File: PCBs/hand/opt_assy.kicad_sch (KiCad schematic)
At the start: 4 parts

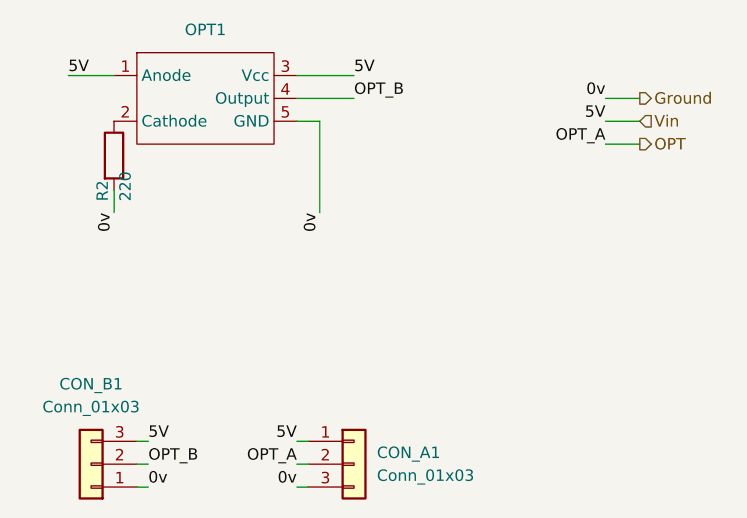
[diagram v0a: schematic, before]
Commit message: Separated Hand B as separate Kicad project. Next up: gerber generation
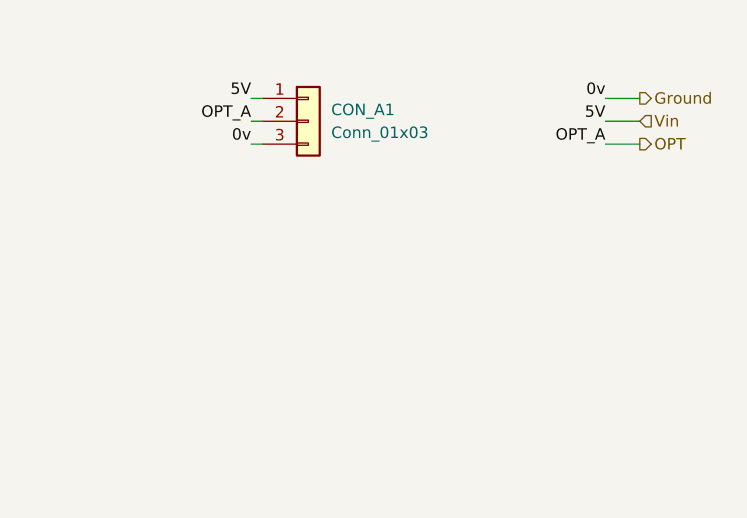
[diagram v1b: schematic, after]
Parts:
- removed CON_B1: Conn_01x03, Connector_PinHeader_2.54mm:PinHeader_1x03_P2.54mm_Vertical, symbol Connector_Generic:Conn_01x03
- removed OPT1: ~, OPB971N51:OPB971N51, symbol OPB971N51:OPB971N51
- removed R2: 220, Resistor_SMD:R_0402_1005Metric, symbol Device:R
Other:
- moved on the sheet: CON_A1
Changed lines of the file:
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@@
 (kicad_sch (version 20230121) (generator eeschema)
   (paper "A5")
-  (wire (pts (xy 85.09 52.07) (xy 85.09 49.53))
-    (stroke (width 0) (type default))
-  )
-  (wire (pts (xy 87.63 80.01) (xy 88.9 80.01))
-    (stroke (width 0) (type default))
-  )
-  (wire (pts (xy 87.63 82.55) (xy 88.9 82.55))
-    (stroke (width 0) (type default))
-  )
-  (wire (pts (xy 105.41 39.37) (xy 111.76 39.37))
-    (stroke (width 0) (type default))
-  )
-  (wire (pts (xy 105.41 36.83) (xy 111.76 36.83))
-    (stroke (width 0) (type default))
-  )
-  (wire (pts (xy 105.41 77.47) (xy 106.68 77.47))
+  (wire (pts (xy 100.33 39.37) (xy 101.6 39.37))
     (stroke (width 0) (type default))
   )
@@
     (stroke (width 0) (type default))
   )
-  (wire (pts (xy 107.95 41.91) (xy 107.95 52.07))
-    (stroke (width 0) (type default))
-  )
-  (wire (pts (xy 105.41 80.01) (xy 106.68 80.01))
+  (wire (pts (xy 100.33 41.91) (xy 101.6 41.91))
     (stroke (width 0) (type default))
   )
@@
     (stroke (width 0) (type default))
   )
-  (wire (pts (xy 87.63 77.47) (xy 88.9 77.47))
-    (stroke (width 0) (type default))
-  )
   (wire (pts (xy 139.7 41.91) (xy 143.51 41.91))
     (stroke (width 0) (type default))
   )
-  (wire (pts (xy 80.01 36.83) (xy 85.09 36.83))
+  (wire (pts (xy 100.33 44.45) (xy 101.6 44.45))
     (stroke (width 0) (type default))
   )
-  (wire (pts (xy 105.41 41.91) (xy 107.95 41.91))
-    (stroke (width 0) (type default))
-  )
-  (wire (pts (xy 105.41 82.55) (xy 106.68 82.55))
-    (stroke (width 0) (type default))
-  )
-  (label "0v" (at 105.41 82.55 180) (fields_autoplaced)
+  (label "0v" (at 100.33 44.45 180) (fields_autoplaced)
     (effects (font (size 1.27 1.27)) (justify right bottom))
   )
-  (label "OPT_B" (at 111.76 39.37 0) (fields_autoplaced)
-    (effects (font (size 1.27 1.27)) (justify left bottom))
-  )
-  (label "OPT_A" (at 105.41 80.01 180) (fields_autoplaced)
+  (label "OPT_A" (at 100.33 41.91 180) (fields_autoplaced)
     (effects (font (size 1.27 1.27)) (justify right bottom))
-  )
-  (label "5V" (at 111.76 36.83 0) (fields_autoplaced)
-    (effects (font (size 1.27 1.27)) (justify left bottom))
-  )
-  (label "5V" (at 88.9 77.47 0) (fields_autoplaced)
-    (effects (font (size 1.27 1.27)) (justify left bottom))
   )
   (label "5V" (at 139.7 41.91 180) (fields_autoplaced)
     (effects (font (size 1.27 1.27)) (justify right bottom))
   )
-  (label "0v" (at 88.9 82.55 0) (fields_autoplaced)
-    (effects (font (size 1.27 1.27)) (justify left bottom))
-  )
-  (label "OPT_B" (at 88.9 80.01 0) (fields_autoplaced)
-    (effects (font (size 1.27 1.27)) (justify left bottom))
-  )
-  (label "5V" (at 105.41 77.47 180) (fields_autoplaced)
+  (label "5V" (at 100.33 39.37 180) (fields_autoplaced)
     (effects (font (size 1.27 1.27)) (justify right bottom))
   )
@@
     (effects (font (size 1.27 1.27)) (justify right bottom))
   )
-  (label "0v" (at 107.95 52.07 270) (fields_autoplaced)
-    (effects (font (size 1.27 1.27)) (justify right bottom))
-  )
-  (label "5V" (at 80.01 36.83 0) (fields_autoplaced)
-    (effects (font (size 1.27 1.27)) (justify left bottom))
-  )
   (label "0v" (at 139.7 39.37 180) (fields_autoplaced)
-    (effects (font (size 1.27 1.27)) (justify right bottom))
-  )
-  (label "0v" (at 85.09 52.07 270) (fields_autoplaced)
     (effects (font (size 1.27 1.27)) (justify right bottom))
   )
@@
     (effects (font (size 1.27 1.27)) (justify left))
   )
-  (symbol (lib_id "Device:R") (at 85.09 45.72 0) (unit 1)
-    (in_bom yes) (on_board yes) (dnp no)
-    (property "Reference" "R2" (at 83.82 50.8 90)
+  (symbol (lib_id "Connector_Generic:Conn_01x03") (at 106.68 41.91 0) (unit 1)
+    (in_bom yes) (on_board yes) (dnp no) (fields_autoplaced)
+    (property "Reference" "CON_A1" (at 109.22 40.64 0)
       (effects (font (size 1.27 1.27)) (justify left))
     )
-    (property "Value" "220" (at 86.36 50.8 90)
+    (property "Value" "Conn_01x03" (at 109.22 43.18 0)
       (effects (font (size 1.27 1.27)) (justify left))
     )
-    (property "Footprint" "Resistor_SMD:R_0402_1005Metric" (at 83.312 45.72 90)
+    (property "Footprint" "Connector_PinHeader_2.54mm:PinHeader_1x03_P2.54mm_Vertical" (at 106.68 41.91 0)
       (effects (font (size 1.27 1.27)) hide)
     )
-    (property "Datasheet" "~" (at 85.09 45.72 0)
-      (effects (font (size 1.27 1.27)) hide)
-    )
-    (pin "1")
-    (pin "2")
-    (instances
-      (project "hand"
-        (path "/5df167e9-440d-40dc-8690-43ffe4e4c50d"
-          (reference "R2") (unit 1)
-        )
-        (path "/5df167e9-440d-40dc-8690-43ffe4e4c50d/0c4cb80d-a6d8-4cad-aec7-41b1541506df"
-          (reference "R2") (unit 1)
-        )
-      )
-    )
-  )
-  (symbol (lib_id "Connector_Generic:Conn_01x03") (at 111.76 80.01 0) (unit 1)
-    (in_bom yes) (on_board yes) (dnp no) (fields_autoplaced)
-    (property "Reference" "CON_A1" (at 114.3 78.74 0)
-      (effects (font (size 1.27 1.27)) (justify left))
-    )
-    (property "Value" "Conn_01x03" (at 114.3 81.28 0)
-      (effects (font (size 1.27 1.27)) (justify left))
-    )
-    (property "Footprint" "Connector_PinHeader_2.54mm:PinHeader_1x03_P2.54mm_Vertical" (at 111.76 80.01 0)
-      (effects (font (size 1.27 1.27)) hide)
-    )
-    (property "Datasheet" "~" (at 111.76 80.01 0)
+    (property "Datasheet" "~" (at 106.68 41.91 0)
       (effects (font (size 1.27 1.27)) hide)
     )
@@
         )
       )
-    )
-  )
-  (symbol (lib_id "OPB971N51:OPB971N51") (at 95.25 39.37 0) (unit 1)
-    (in_bom yes) (on_board yes) (dnp no) (fields_autoplaced)
-    (property "Reference" "OPT1" (at 95.25 31.75 0)
-      (effects (font (size 1.27 1.27)))
-    )
-    (property "Value" "~" (at 93.98 45.72 0)
-      (effects (font (size 1.27 1.27)))
-    )
-    (property "Footprint" "OPB971N51:OPB971N51" (at 93.98 45.72 0)
-      (effects (font (size 1.27 1.27)) hide)
-    )
-    (property "Datasheet" "" (at 93.98 45.72 0)
-      (effects (font (size 1.27 1.27)) hide)
-    )
-    (pin "1")
-    (pin "2")
-    (pin "3")
-    (pin "4")
-    (pin "5")
-    (instances
-      (project "hand"
-        (path "/5df167e9-440d-40dc-8690-43ffe4e4c50d"
-          (reference "OPT1") (unit 1)
-        )
-        (path "/5df167e9-440d-40dc-8690-43ffe4e4c50d/0c4cb80d-a6d8-4cad-aec7-41b1541506df"
-          (reference "OPT1") (unit 1)
-        )
-      )
-    )
-  )
-  (symbol (lib_id "Connector_Generic:Conn_01x03") (at 82.55 80.01 180) (unit 1)
-    (in_bom yes) (on_board yes) (dnp no) (fields_autoplaced)
-    (property "Reference" "CON_B1" (at 82.55 71.12 0)
-      (effects (font (size 1.27 1.27)))
-    )
-    (property "Value" "Conn_01x03" (at 82.55 73.66 0)
-      (effects (font (size 1.27 1.27)))
-    )
-    (property "Footprint" "Connector_PinHeader_2.54mm:PinHeader_1x03_P2.54mm_Vertical" (at 82.55 80.01 0)
-      (effects (font (size 1.27 1.27)) hide)
-    )
-    (property "Datasheet" "~" (at 82.55 80.01 0)
-      (effects (font (size 1.27 1.27)) hide)
-    )
-    (pin "1")
-    (pin "2")
-    (pin "3")
-    (instances
-      (project "hand"
-        (path "/5df167e9-440d-40dc-8690-43ffe4e4c50d"
-          (reference "CON_B1") (unit 1)
-        )
-        (path "/5df167e9-440d-40dc-8690-43ffe4e4c50d/0c4cb80d-a6d8-4cad-aec7-41b1541506df"
-          (reference "CON_B1") (unit 1)
-        )
-      )

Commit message: Added pcb pdfs
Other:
- moved on the sheet: CON_A1
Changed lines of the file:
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@@
 (kicad_sch (version 20230121) (generator eeschema)
   (paper "A5")
-  (wire (pts (xy 100.33 39.37) (xy 101.6 39.37))
+  (wire (pts (xy 81.28 64.77) (xy 82.55 64.77))
     (stroke (width 0) (type default))
   )
-  (wire (pts (xy 139.7 44.45) (xy 143.51 44.45))
+  (wire (pts (xy 120.65 69.85) (xy 124.46 69.85))
     (stroke (width 0) (type default))
   )
-  (wire (pts (xy 100.33 41.91) (xy 101.6 41.91))
+  (wire (pts (xy 81.28 67.31) (xy 82.55 67.31))
     (stroke (width 0) (type default))
   )
-  (wire (pts (xy 139.7 39.37) (xy 143.51 39.37))
+  (wire (pts (xy 120.65 64.77) (xy 124.46 64.77))
     (stroke (width 0) (type default))
   )
-  (wire (pts (xy 139.7 41.91) (xy 143.51 41.91))
+  (wire (pts (xy 120.65 67.31) (xy 124.46 67.31))
     (stroke (width 0) (type default))
   )
-  (wire (pts (xy 100.33 44.45) (xy 101.6 44.45))
+  (wire (pts (xy 81.28 69.85) (xy 82.55 69.85))
     (stroke (width 0) (type default))
   )
-  (label "0v" (at 100.33 44.45 180) (fields_autoplaced)
+  (label "0v" (at 81.28 69.85 180) (fields_autoplaced)
     (effects (font (size 1.27 1.27)) (justify right bottom))
   )
-  (label "OPT_A" (at 100.33 41.91 180) (fields_autoplaced)
+  (label "OPT_A" (at 81.28 67.31 180) (fields_autoplaced)
     (effects (font (size 1.27 1.27)) (justify right bottom))
   )
-  (label "5V" (at 139.7 41.91 180) (fields_autoplaced)
+  (label "5V" (at 120.65 67.31 180) (fields_autoplaced)
     (effects (font (size 1.27 1.27)) (justify right bottom))
   )
-  (label "5V" (at 100.33 39.37 180) (fields_autoplaced)
+  (label "5V" (at 81.28 64.77 180) (fields_autoplaced)
     (effects (font (size 1.27 1.27)) (justify right bottom))
   )
-  (label "OPT_A" (at 139.7 44.45 180) (fields_autoplaced)
+  (label "OPT_A" (at 120.65 69.85 180) (fields_autoplaced)
     (effects (font (size 1.27 1.27)) (justify right bottom))
   )
-  (label "0v" (at 139.7 39.37 180) (fields_autoplaced)
+  (label "0v" (at 120.65 64.77 180) (fields_autoplaced)
     (effects (font (size 1.27 1.27)) (justify right bottom))
   )
-  (hierarchical_label "Ground" (shape output) (at 143.51 39.37 0) (fields_autoplaced)
+  (hierarchical_label "Ground" (shape output) (at 124.46 64.77 0) (fields_autoplaced)
     (effects (font (size 1.27 1.27)) (justify left))
   )
-  (hierarchical_label "OPT" (shape output) (at 143.51 44.45 0) (fields_autoplaced)
+  (hierarchical_label "OPT" (shape output) (at 124.46 69.85 0) (fields_autoplaced)
     (effects (font (size 1.27 1.27)) (justify left))
   )
-  (hierarchical_label "Vin" (shape input) (at 143.51 41.91 0) (fields_autoplaced)
+  (hierarchical_label "Vin" (shape input) (at 124.46 67.31 0) (fields_autoplaced)
     (effects (font (size 1.27 1.27)) (justify left))
   )
-  (symbol (lib_id "Connector_Generic:Conn_01x03") (at 106.68 41.91 0) (unit 1)
+  (symbol (lib_id "Connector_Generic:Conn_01x03") (at 87.63 67.31 0) (unit 1)
     (in_bom yes) (on_board yes) (dnp no) (fields_autoplaced)
-    (property "Reference" "CON_A1" (at 109.22 40.64 0)
+    (property "Reference" "CON_A1" (at 90.17 66.04 0)
       (effects (font (size 1.27 1.27)) (justify left))
     )
-    (property "Value" "Conn_01x03" (at 109.22 43.18 0)
+    (property "Value" "Conn_01x03" (at 90.17 68.58 0)
       (effects (font (size 1.27 1.27)) (justify left))
     )
-    (property "Footprint" "Connector_PinHeader_2.54mm:PinHeader_1x03_P2.54mm_Vertical" (at 106.68 41.91 0)
+    (property "Footprint" "Connector_PinHeader_2.54mm:PinHeader_1x03_P2.54mm_Vertical" (at 87.63 67.31 0)
       (effects (font (size 1.27 1.27)) hide)
     )
-    (property "Datasheet" "~" (at 106.68 41.91 0)
+    (property "Datasheet" "~" (at 87.63 67.31 0)
       (effects (font (size 1.27 1.27)) hide)
     )
@@
     (instances
       (project "hand"
-        (path "/5df167e9-440d-40dc-8690-43ffe4e4c50d"
-          (reference "CON_A1") (unit 1)
-        )
         (path "/5df167e9-440d-40dc-8690-43ffe4e4c50d/0c4cb80d-a6d8-4cad-aec7-41b1541506df"
           (reference "CON_A1") (unit 1)
